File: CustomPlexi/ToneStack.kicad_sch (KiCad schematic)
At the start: 7 parts, among them U1 TL074

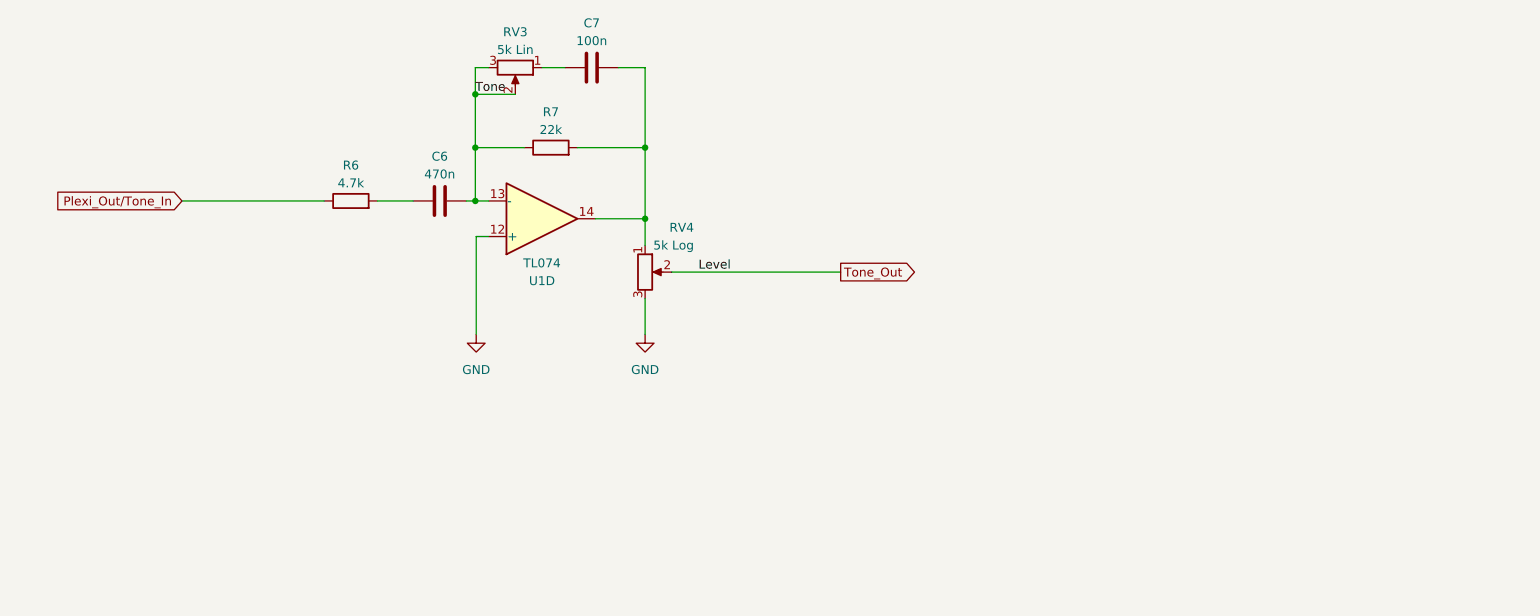
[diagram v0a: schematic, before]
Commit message: Signal chain ok except separated volumes
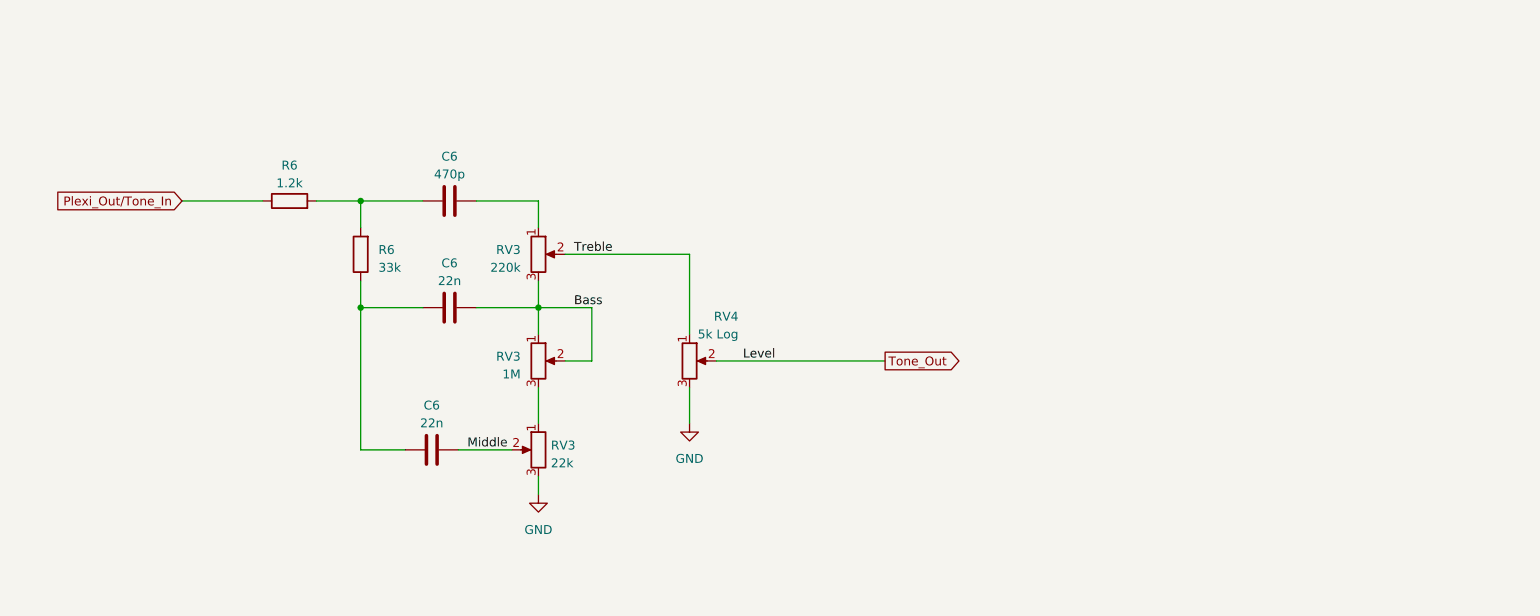
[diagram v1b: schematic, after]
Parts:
- removed C7: 100n, Capacitor_SMD:C_0603_1608Metric_Pad1.08x0.95mm_HandSolder, symbol PCM_Capacitor_AKL:C_0603
- removed R7: 22k, Resistor_SMD:R_0603_1608Metric_Pad0.98x0.95mm_HandSolder, symbol PCM_Resistor_AKL:R_0603
- removed U1: TL074, symbol Amplifier_Operational:TL074
- added C6 (x2): 22n, Capacitor_SMD_AKL:C_0603_1608Metric, symbol PCM_Capacitor_AKL:C_0603
- added R6: 33k, Resistor_SMD_AKL:R_0603_1608Metric, symbol PCM_Resistor_AKL:R_0603
- added RV3: 1M, symbol Device:R_Potentiometer
- added RV3: 22k, symbol Device:R_Potentiometer
- C6: value 470n -> 470p; footprint Capacitor_SMD:C_0603_1608Metric_Pad1.08x0.95mm_HandSolder -> Capacitor_SMD_AKL:C_0603_1608Metric
- R6: value 4.7k -> 1.2k; footprint Resistor_SMD:R_0603_1608Metric_Pad0.98x0.95mm_HandSolder -> Resistor_SMD_AKL:R_0603_1608Metric
- RV3: value 5k Lin -> 220k
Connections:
- net GND: now also RV3.3
- net at C6.1, R6.2: now also R6.2
- net Treble: now reaches RV4.1
- net Treble: now also RV3.2
- net at RV3.1: now also C6.2
- removed net Tone: C6.2, RV3.2, RV3.3
- new net: RV3.1, RV3.3
- new net: C6.1, C6.1, R6.1
- new net Bass: C6.2, RV3.1, RV3.2, RV3.3
- new net Middle: C6.2, RV3.2
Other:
- moved on the sheet: C6, R6, RV3, RV4

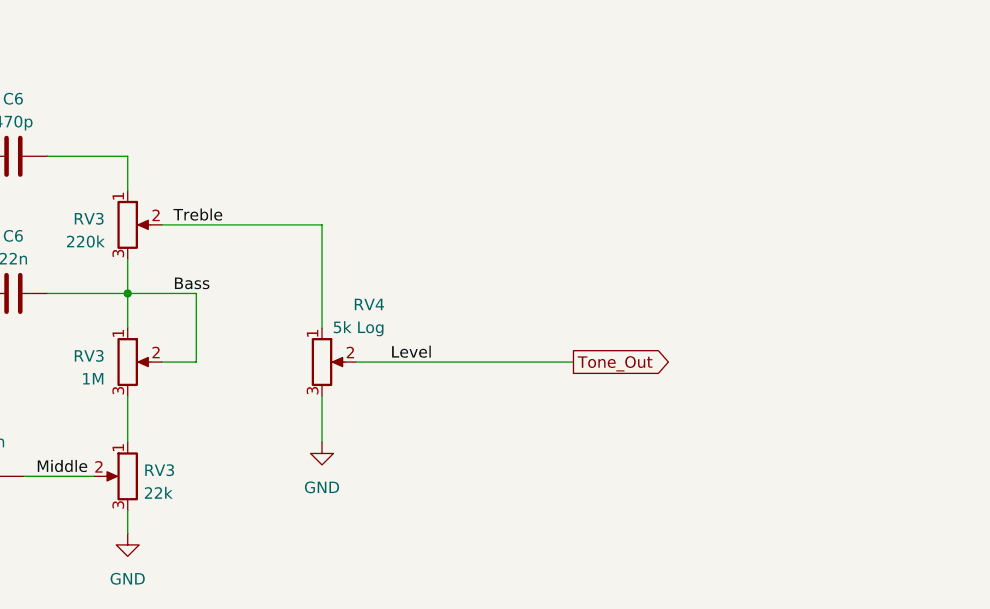
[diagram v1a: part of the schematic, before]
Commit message: crunch and leadh channel has separated level control
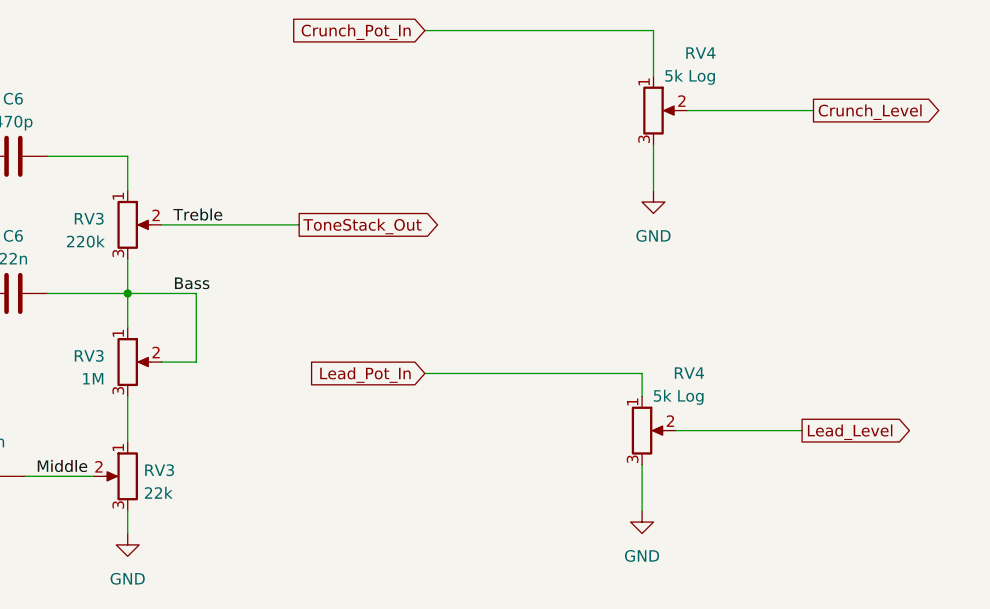
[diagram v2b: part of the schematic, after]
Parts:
- added RV4: 5k Log, symbol Device:R_Potentiometer
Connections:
- net GND: now also RV4.3
- net Tone_Out renamed Crunch_Level
- net Treble renamed Crunch_Pot_In
- net Crunch_Pot_In: no longer RV3.2
- new net Lead_Level: RV4.2
- new net Lead_Pot_In: RV4.1
- new net ToneStack_Out: RV3.2
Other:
- moved on the sheet: RV4
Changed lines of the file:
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@@
   (junction (at 105.41 93.98) (diameter 0) (color 0 0 0 0)
   )
-  (wire (pts (xy 156.21 101.6) (xy 180.34 101.6))
+  (wire (pts (xy 207.01 73.66) (xy 193.04 73.66))
     (stroke (width 0) (type default))
   )
@@
     (stroke (width 0) (type default))
   )
-  (wire (pts (xy 152.4 86.36) (xy 152.4 97.79))
+  (wire (pts (xy 187.96 102.87) (xy 187.96 105.41))
     (stroke (width 0) (type default))
   )
@@
     (stroke (width 0) (type default))
   )
-  (wire (pts (xy 152.4 105.41) (xy 152.4 110.49))
+  (wire (pts (xy 189.23 77.47) (xy 189.23 82.55))
     (stroke (width 0) (type default))
   )
@@
     (stroke (width 0) (type default))
   )
+  (wire (pts (xy 187.96 113.03) (xy 187.96 118.11))
+    (stroke (width 0) (type default))
+  )
   (wire (pts (xy 99.06 78.74) (xy 105.41 78.74))
     (stroke (width 0) (type default))
@@
     (stroke (width 0) (type default))
   )
-  (wire (pts (xy 134.62 86.36) (xy 152.4 86.36))
+  (wire (pts (xy 134.62 86.36) (xy 149.86 86.36))
+    (stroke (width 0) (type default))
+  )
+  (wire (pts (xy 163.83 64.77) (xy 189.23 64.77))
     (stroke (width 0) (type default))
   )
@@
     (stroke (width 0) (type default))
   )
+  (wire (pts (xy 163.83 102.87) (xy 187.96 102.87))
+    (stroke (width 0) (type default))
+  )
   (wire (pts (xy 130.81 93.98) (xy 138.43 93.98))
     (stroke (width 0) (type default))
@@
     (stroke (width 0) (type default))
   )
+  (wire (pts (xy 205.74 109.22) (xy 191.77 109.22))
+    (stroke (width 0) (type default))
+  )
   (wire (pts (xy 138.43 93.98) (xy 138.43 101.6))
+    (stroke (width 0) (type default))
+  )
+  (wire (pts (xy 189.23 64.77) (xy 189.23 69.85))
     (stroke (width 0) (type default))
   )
@@
     (effects (font (size 1.27 1.27)) (justify left bottom))
   )
-  (label "Level" (at 160.02 101.6 0) (fields_autoplaced)
-    (effects (font (size 1.27 1.27)) (justify left bottom))
+  (global_label "Lead_Pot_In" (shape input) (at 163.83 102.87 180) (fields_autoplaced)
+    (effects (font (size 1.27 1.27)) (justify right))
+    (property "Intersheetrefs" "${INTERSHEET_REFS}" (at 149.6758 102.87 0)
+      (effects (font (size 1.27 1.27)) (justify right) hide)
+    )
+  )
+  (global_label "ToneStack_Out" (shape output) (at 149.86 86.36 0) (fields_autoplaced)
+    (effects (font (size 1.27 1.27)) (justify left))
+    (property "Intersheetrefs" "${INTERSHEET_REFS}" (at 166.4937 86.36 0)
+      (effects (font (size 1.27 1.27)) (justify left) hide)
+    )
+  )
+  (global_label "Lead_Level" (shape output) (at 205.74 109.22 0) (fields_autoplaced)
+    (effects (font (size 1.27 1.27)) (justify left))
+    (property "Intersheetrefs" "${INTERSHEET_REFS}" (at 218.8662 109.22 0)
+      (effects (font (size 1.27 1.27)) (justify left) hide)
+    )
   )
   (global_label "Plexi_Out{slash}Tone_In" (shape input) (at 79.883 78.74 180) (fields_autoplaced)
@@
     )
   )
-  (global_label "Tone_Out" (shape output) (at 180.34 101.6 0) (fields_autoplaced)
+  (global_label "Crunch_Level" (shape output) (at 207.01 73.66 0) (fields_autoplaced)
     (effects (font (size 1.27 1.27)) (justify left))
-    (property "Intersheetrefs" "${INTERSHEET_REFS}" (at 191.7728 101.6 0)
+    (property "Intersheetrefs" "${INTERSHEET_REFS}" (at 222.3133 73.66 0)
       (effects (font (size 1.27 1.27)) (justify left) hide)
     )
   )
-  (symbol (lib_id "power:GND") (at 152.4 110.49 0) (unit 1)
-    (in_bom yes) (on_board yes) (dnp no) (fields_autoplaced)
-    (property "Reference" "#PWR02" (at 152.4 116.84 0)
-      (effects (font (size 1.27 1.27)) hide)
-    )
-    (property "Value" "GND" (at 152.4 115.57 0)
-      (effects (font (size 1.27 1.27)))
-    )
-    (property "Footprint" "" (at 152.4 110.49 0)
-      (effects (font (size 1.27 1.27)) hide)
-    )
-    (property "Datasheet" "" (at 152.4 110.49 0)
+  (global_label "Crunch_Pot_In" (shape input) (at 163.83 64.77 180) (fields_autoplaced)
+    (effects (font (size 1.27 1.27)) (justify right))
+    (property "Intersheetrefs" "${INTERSHEET_REFS}" (at 147.4987 64.77 0)
+      (effects (font (size 1.27 1.27)) (justify right) hide)
+    )
+  )
+  (symbol (lib_id "power:GND") (at 189.23 82.55 0) (unit 1)
+    (in_bom yes) (on_board yes) (dnp no) (fields_autoplaced)
+    (property "Reference" "#PWR02" (at 189.23 88.9 0)
+      (effects (font (size 1.27 1.27)) hide)
+    )
+    (property "Value" "GND" (at 189.23 87.63 0)
+      (effects (font (size 1.27 1.27)))
+    )
+    (property "Footprint" "" (at 189.23 82.55 0)
+      (effects (font (size 1.27 1.27)) hide)
+    )
+    (property "Datasheet" "" (at 189.23 82.55 0)
       (effects (font (size 1.27 1.27)) hide)
     )
@@
         (path "/cb47f45c-6a2b-402e-a3a9-bf4992e06e45/d67dc5e3-b5e6-4ced-a0aa-c1f6a7e7b9d1"
           (reference "RV7") (unit 1)
+        )
+      )
+    )
+  )
+  (symbol (lib_id "power:GND") (at 187.96 118.11 0) (unit 1)
+    (in_bom yes) (on_board yes) (dnp no) (fields_autoplaced)
+    (property "Reference" "#PWR02" (at 187.96 124.46 0)
+      (effects (font (size 1.27 1.27)) hide)
+    )
+    (property "Value" "GND" (at 187.96 123.19 0)
+      (effects (font (size 1.27 1.27)))
+    )
+    (property "Footprint" "" (at 187.96 118.11 0)
+      (effects (font (size 1.27 1.27)) hide)
+    )
+    (property "Datasheet" "" (at 187.96 118.11 0)
+      (effects (font (size 1.27 1.27)) hide)
+    )
+    (pin "1")
+    (instances
+      (project "CustomPlexi"
+        (path "/cb47f45c-6a2b-402e-a3a9-bf4992e06e45"
+          (reference "#PWR02") (unit 1)
+        )
+        (path "/cb47f45c-6a2b-402e-a3a9-bf4992e06e45/bb03f90a-acf2-4514-8da0-ce840f9be904"
+          (reference "#PWR03") (unit 1)
+        )
+        (path "/cb47f45c-6a2b-402e-a3a9-bf4992e06e45/d67dc5e3-b5e6-4ced-a0aa-c1f6a7e7b9d1"
+          (reference "#PWR018") (unit 1)
+        )
+      )
+    )
+  )
+  (symbol (lib_id "Device:R_Potentiometer") (at 187.96 109.22 0) (unit 1)
+    (in_bom yes) (on_board yes) (dnp no)
+    (property "Reference" "RV4" (at 194.945 102.87 0)
+      (effects (font (size 1.27 1.27)) (justify right))
+    )
+    (property "Value" "5k Log" (at 194.945 105.41 0)
+      (effects (font (size 1.27 1.27)) (justify right))
+    )
+    (property "Footprint" "" (at 187.96 109.22 0)
+      (effects (font (size 1.27 1.27)) hide)
+    )
+    (property "Datasheet" "~" (at 187.96 109.22 0)
+      (effects (font (size 1.27 1.27)) hide)
+    )
+    (pin "1")
+    (pin "2")
+    (pin "3")
+    (instances
+      (project "CustomPlexi"
+        (path "/cb47f45c-6a2b-402e-a3a9-bf4992e06e45"
+          (reference "RV4") (unit 1)
+        )
+        (path "/cb47f45c-6a2b-402e-a3a9-bf4992e06e45/d67dc5e3-b5e6-4ced-a0aa-c1f6a7e7b9d1"
+          (reference "RV10") (unit 1)
         )
       )
@@
     )
   )
-  (symbol (lib_id "Device:R_Potentiometer") (at 152.4 101.6 0) (unit 1)
+  (symbol (lib_id "Device:R_Potentiometer") (at 189.23 73.66 0) (unit 1)
     (in_bom yes) (on_board yes) (dnp no)
-    (property "Reference" "RV4" (at 159.385 95.25 0)
-      (effects (font (size 1.27 1.27)) (justify right))
-    )
-    (property "Value" "5k Log" (at 159.385 97.79 0)
-      (effects (font (size 1.27 1.27)) (justify right))
-    )
-    (property "Footprint" "" (at 152.4 101.6 0)
-      (effects (font (size 1.27 1.27)) hide)
-    )
-    (property "Datasheet" "~" (at 152.4 101.6 0)
-      (effects (font (size 1.27 1.27)) hide)
-    )
+    (property "Reference" "RV4" (at 196.215 67.31 0)
+      (effects (font (size 1.27 1.27)) (justify right))
+    )
+    (property "Value" "5k Log" (at 196.215 69.85 0)
+      (effects (font (size 1.27 1.27)) (justify right))
+    )
+    (property "Footprint" "" (at 189.23 73.66 0)
+      (effects (font (size 1.27 1.27)) hide)
+    )
+    (property "Datasheet" "~" (at 189.23 73.66 0)
+      (effects (font (size 1.27 1.27)) hide)
+    )

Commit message: commit
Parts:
- added SW5: Plexi Channel Select, symbol CustomLib:SW_SPDT_x4
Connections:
- net Crunch_Level renamed Crunch Level
- net Crunch Level: now also SW5.1
- net Crunch_Pot_In: no longer names the net of RV4.1
- net Crunch_Pot_In: now also SW5.1
- net Lead_Level renamed Lead Level
- net Lead Level: now also SW5.3
- net Lead_Pot_In: no longer names the net of RV4.1
- net Lead_Pot_In: now also SW5.3
- net ToneStack_Out renamed Treble
- net Treble: now also SW5.2
- new net Tone_Out: SW5.2
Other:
- moved on the sheet: RV4

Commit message: switches reviewed
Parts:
- removed unit 4 of SW5
- added SW4: Pedal Enable, symbol CustomLib:SW_SPDT_x3
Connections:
- net Tone_Out: no longer names the net of SW5.2
- net Tone_Out: now also SW4.1
- new net Pedal_SC: SW4.3
- new net Tone_Out/Boost_In: SW4.2
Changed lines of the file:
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@@
+    (stroke (width 0) (type default))
+  )
+  (wire (pts (xy 209.55 97.79) (xy 223.52 97.79))
     (stroke (width 0) (type default))
   )
@@
     (stroke (width 0) (type default))
   )
+  (wire (pts (xy 223.52 102.87) (xy 223.52 134.62))
+    (stroke (width 0) (type default))
+  )
   (wire (pts (xy 170.18 99.06) (xy 170.18 104.14))
     (stroke (width 0) (type default))
@@
     (stroke (width 0) (type default))
   )
+  (wire (pts (xy 81.28 134.62) (xy 223.52 134.62))
+    (stroke (width 0) (type default))
+  )
   (wire (pts (xy 119.38 114.3) (xy 127 114.3))
     (stroke (width 0) (type default))
@@
     (stroke (width 0) (type default))
   )
+  (wire (pts (xy 233.68 100.33) (xy 247.65 100.33))
+    (stroke (width 0) (type default))
+  )
   (wire (pts (xy 138.43 93.98) (xy 138.43 101.6))
     (stroke (width 0) (type default))
@@
     (stroke (width 0) (type default))
   )
-  (wire (pts (xy 209.55 97.79) (xy 218.44 97.79))
-    (stroke (width 0) (type default))
-  )
   (wire (pts (xy 162.56 95.25) (xy 162.56 100.33))
     (stroke (width 0) (type default))
@@
     (effects (font (size 1.27 1.27)) (justify left bottom))
   )
-  (global_label "Tone_Out" (shape output) (at 218.44 97.79 0) (fields_autoplaced)
+  (global_label "Pedal_SC" (shape input) (at 81.28 134.62 180) (fields_autoplaced)
+    (effects (font (size 1.27 1.27)) (justify right))
+    (property "Intersheetrefs" "${INTERSHEET_REFS}" (at 69.6053 134.62 0)
+      (effects (font (size 1.27 1.27)) (justify right) hide)
+    )
+  )
+  (global_label "Tone_Out{slash}Boost_In" (shape output) (at 247.65 100.33 0) (fields_autoplaced)
     (effects (font (size 1.27 1.27)) (justify left))
-    (property "Intersheetrefs" "${INTERSHEET_REFS}" (at 229.8728 97.79 0)
+    (property "Intersheetrefs" "${INTERSHEET_REFS}" (at 268.4565 100.33 0)
       (effects (font (size 1.27 1.27)) (justify left) hide)
     )
@@
     )
   )
+  (symbol (lib_id "CustomLib:SW_SPDT_x3") (at 228.6 100.33 0) (mirror y) (unit 2)
+    (in_bom yes) (on_board yes) (dnp no)
+    (property "Reference" "SW4" (at 228.6 90.17 0)
+      (effects (font (size 1.27 1.27)))
+    )
+    (property "Value" "Pedal Enable" (at 228.6 92.71 0)
+      (effects (font (size 1.27 1.27)))
+    )
+    (property "Footprint" "" (at 227.33 95.25 0)
+      (effects (font (size 1.27 1.27)) hide)
+    )
+    (property "Datasheet" "" (at 227.33 95.25 0)
+      (effects (font (size 1.27 1.27)) hide)
+    )
+    (pin "1")
+    (pin "2")
+    (pin "3")
+    (pin "1")
+    (pin "2")
+    (pin "3")
+    (pin "1")
+    (pin "2")
+    (pin "3")
+    (instances
+      (project "CustomPlexi"
+        (path "/cb47f45c-6a2b-402e-a3a9-bf4992e06e45/46194796-04b4-4b0f-a843-2a3656b84ab8"
+          (reference "SW4") (unit 2)
+        )
+        (path "/cb47f45c-6a2b-402e-a3a9-bf4992e06e45/d67dc5e3-b5e6-4ced-a0aa-c1f6a7e7b9d1"
+          (reference "SW4") (unit 2)
+        )
+      )
+    )
+  )
   (symbol (lib_id "power:GND") (at 158.75 104.14 0) (unit 1)
     (in_bom yes) (on_board yes) (dnp no) (fields_autoplaced)
@@
         )
       )
-    )
-  )
-  (symbol (lib_id "CustomLib:SW_SPDT_x4") (at 240.03 77.47 0) (unit 4)
-    (in_bom yes) (on_board yes) (dnp no)
-    (property "Reference" "SW5" (at 242.57 68.58 0)
-      (effects (font (size 1.27 1.27)))
-    )
-    (property "Value" "Plexi Channel Select" (at 242.57 71.12 0)
-      (effects (font (size 1.27 1.27)))
-    )
-    (property "Footprint" "" (at 241.3 72.39 0)
-      (effects (font (size 1.27 1.27)) hide)
-    )
-    (property "Datasheet" "" (at 241.3 72.39 0)
-      (effects (font (size 1.27 1.27)) hide)
-    )
-    (pin "1")
-    (pin "2")
-    (pin "3")
-    (pin "1")
-    (pin "2")
-    (pin "3")
-    (pin "1")
-    (pin "2")
-    (pin "3")
-    (pin "1")
-    (pin "2")
-    (pin "3")
-    (instances
-      (project "CustomPlexi"
-        (path "/cb47f45c-6a2b-402e-a3a9-bf4992e06e45/bb03f90a-acf2-4514-8da0-ce840f9be904"
-          (reference "SW5") (unit 4)
-        )
-        (path "/cb47f45c-6a2b-402e-a3a9-bf4992e06e45/d67dc5e3-b5e6-4ced-a0aa-c1f6a7e7b9d1"
-          (reference "SW5") (unit 4)
-        )
-      )
